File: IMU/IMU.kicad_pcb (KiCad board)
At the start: 2 copper layers, 32.2 x 21.5 mm, 7 parts, among them IC1 ICM-42688-P, J2 IMU

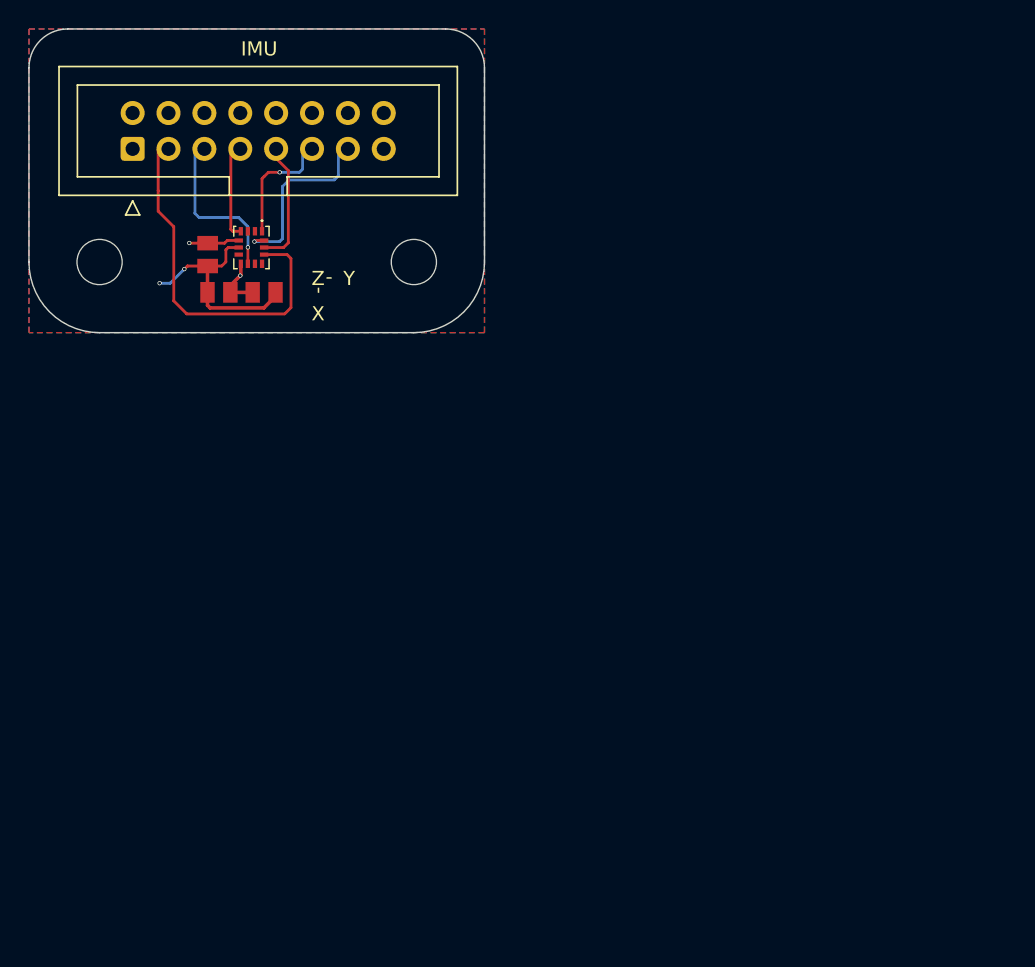
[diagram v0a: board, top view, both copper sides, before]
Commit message: fix all via to 0.45/0.3 mm
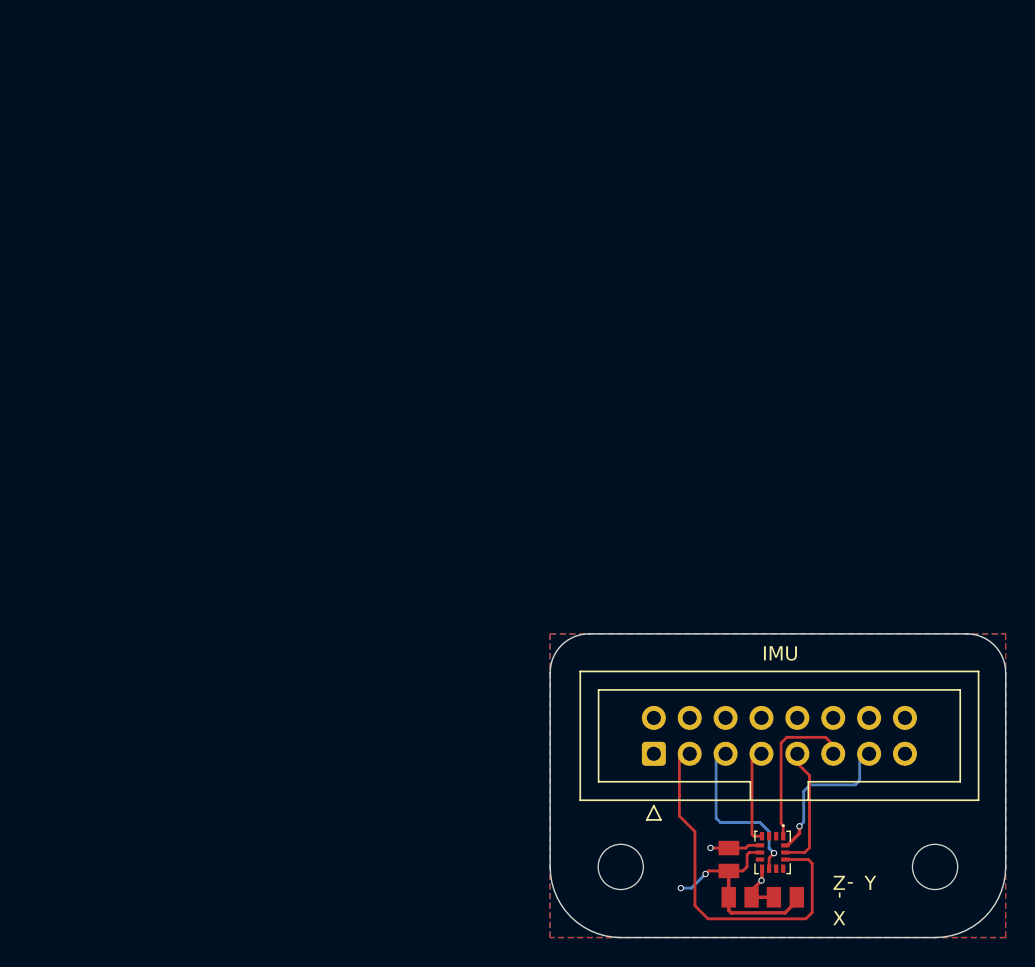
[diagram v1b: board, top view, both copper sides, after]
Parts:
- moved C3 56.5 mm to (147.3, 108.5)
- moved H1 56.5 mm to (161.9, 109.1)
- moved H2 56.5 mm to (139.7, 109.1)
- moved IC1 56.5 mm to (150.4, 108.0)
- moved C1 56.5 mm to (151.3, 111.2)
- moved J2 56.5 mm to (142.0, 101.1)
- moved C2 56.5 mm to (148.1, 111.2)
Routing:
- net SDO: track 8.31 -> 11.4 mm, vias 1 -> 0
- net SDI: track 12.7 -> 10.6 mm
